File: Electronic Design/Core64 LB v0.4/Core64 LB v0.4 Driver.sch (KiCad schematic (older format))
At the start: 63 parts, among them Q4 MMBT4401LT1G

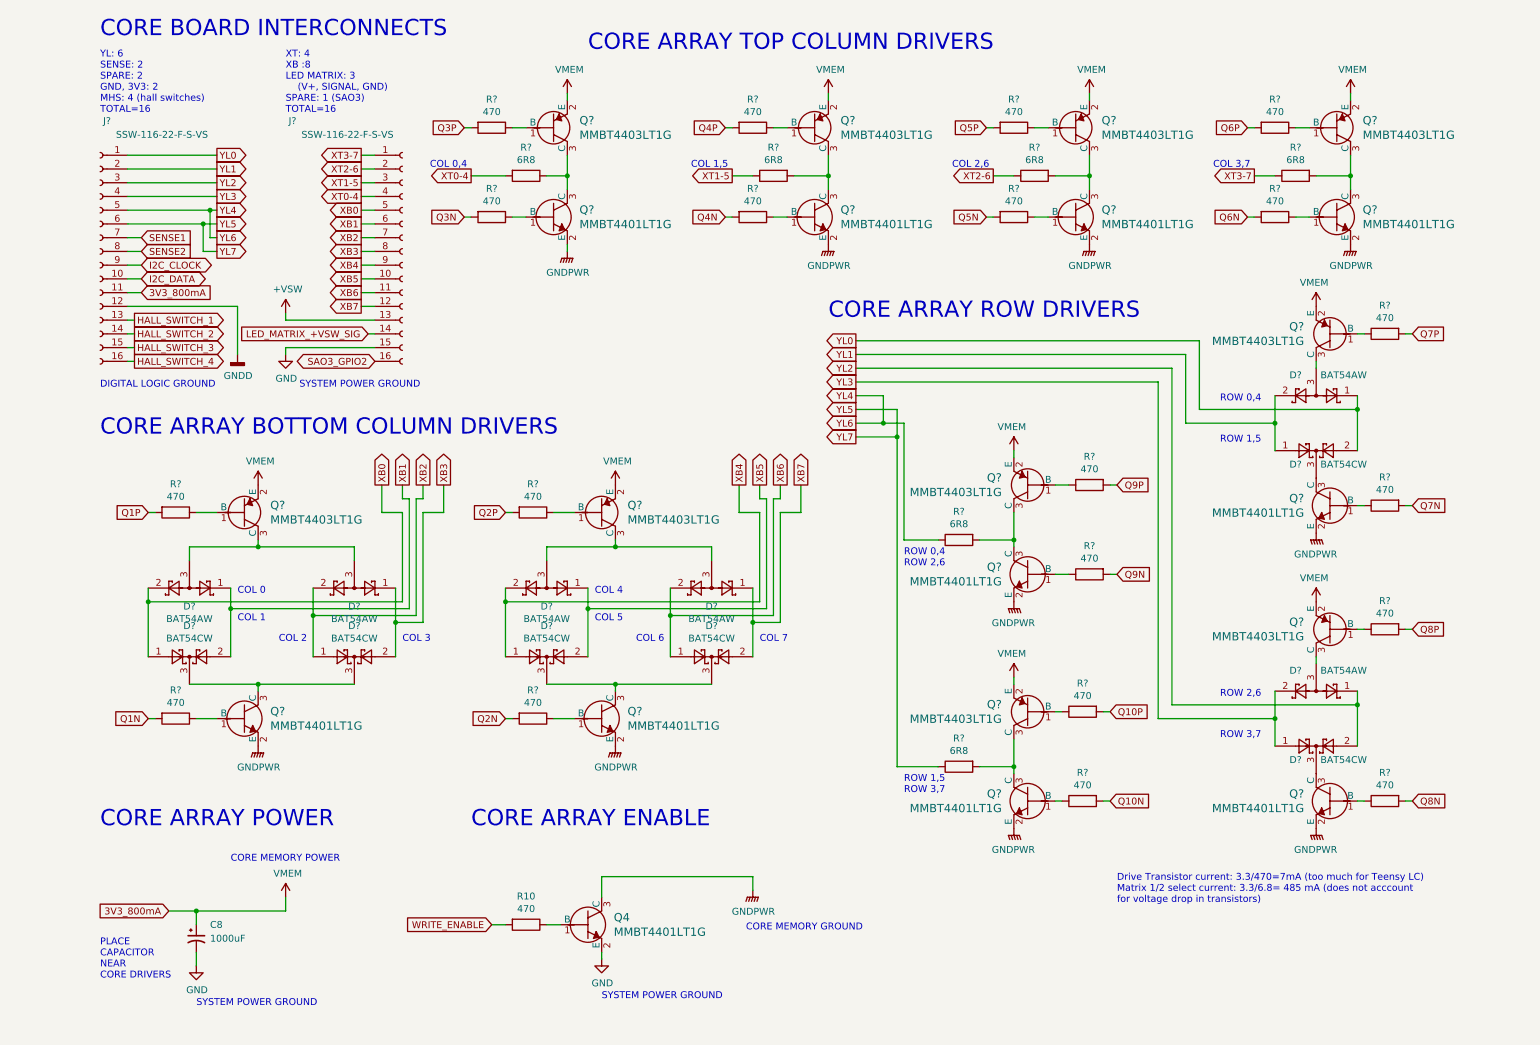
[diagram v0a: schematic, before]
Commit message: Correct Logic Board filenames to LB from CB
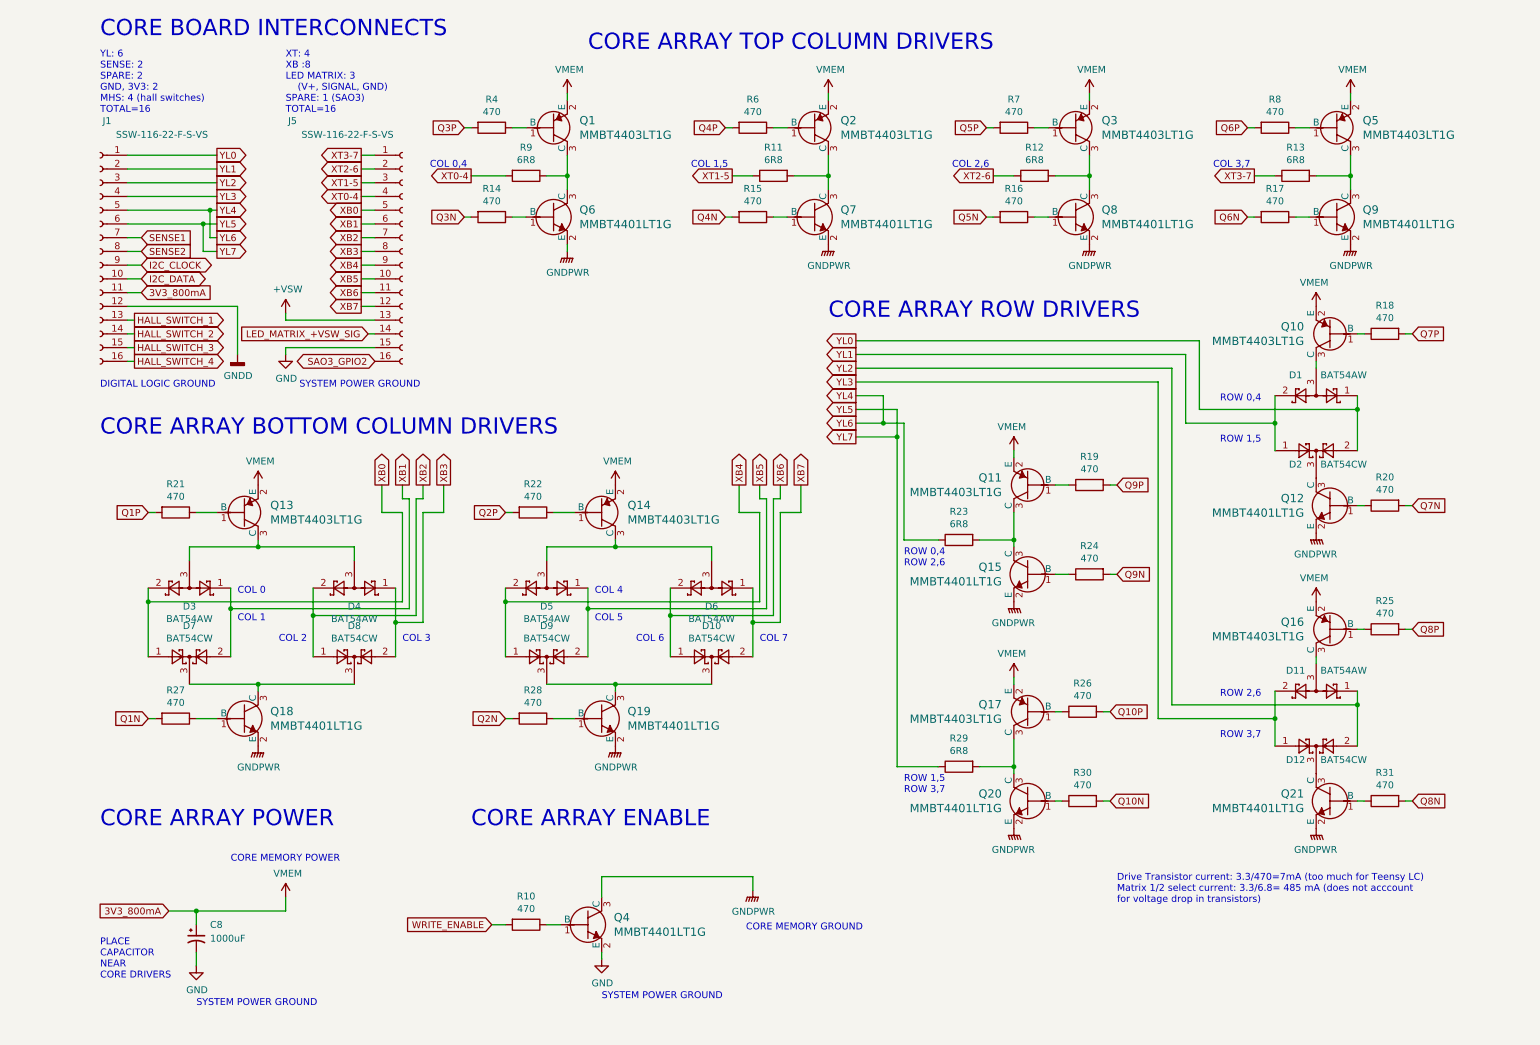
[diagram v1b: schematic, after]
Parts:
- gave numbers to parts that had none: 60

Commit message: Add regulator and battery connector data sheets, footprints, symbols
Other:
- note added: "All non-polarized capacitors are ceramic unless otherwise noted."
- note added: "TO DO: Choose BIG CAP footprint"
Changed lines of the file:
@@
 Wire Wire Line
 	3950 2250 3950 2300
+Text Notes 6300 6750 0    50   ~ 0
+All non-polarized capacitors are ceramic unless otherwise noted.
+Text Notes -100 7450 0    157  ~ 31
+TO DO: Choose BIG CAP footprint
 $EndSCHEMATC

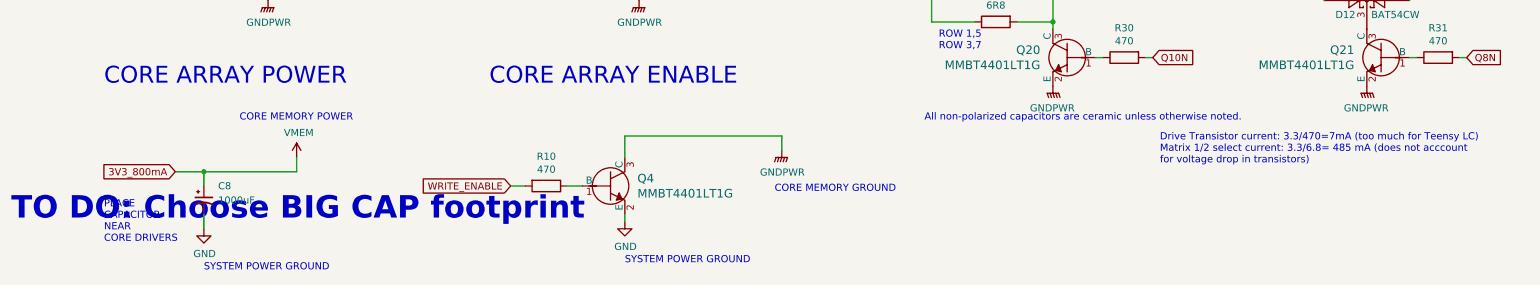
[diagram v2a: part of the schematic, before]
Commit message: Complete LB power schematic, add 3-to-8 decoder
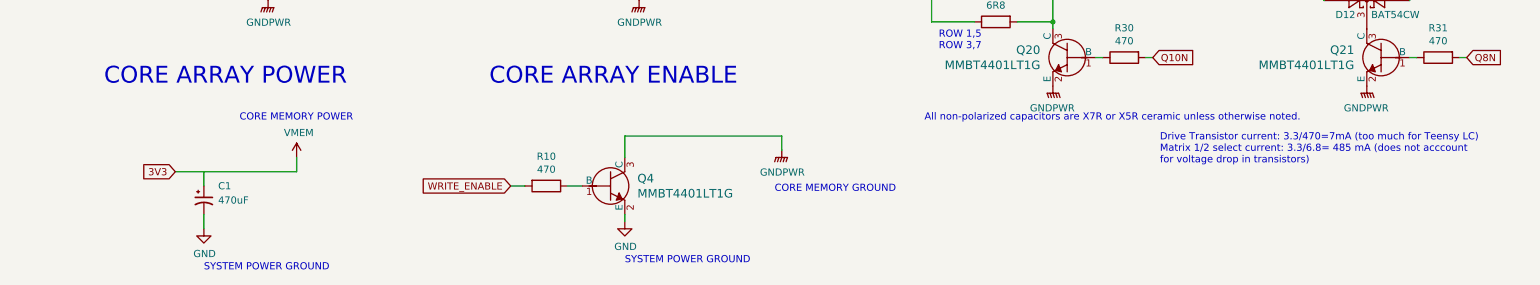
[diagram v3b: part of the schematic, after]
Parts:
- removed C8: 1000uF, Capacitor_SMD:CP_Elec_10x10, symbol Device:CP1_Small
- added C1: 470uF, Capacitor_SMD:CP_Elec_10x10, symbol Device:CP1_Small
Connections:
- net GND: now also C1.2
- net VMEM: no longer J1.11 (Pin_11)
- new net 3V3_800mA: J1.11 (Pin_11)
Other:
- note added: "All non-polarized capacitors are X7R or X5R ceramic unless otherwise noted."
- note removed: "All non-polarized capacitors are ceramic unless otherwise noted."
- note removed: "PLACE\nCAPACITOR\nNEAR\nCORE DRIVERS"
- note removed: "TO DO: Choose BIG CAP footprint"
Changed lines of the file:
@@
 CORE MEMORY POWER
 Text GLabel 1050 7100 0    50   Input ~ 0
-3V3_800mA
+3V3
 $Comp
 L power:GND #PWR?
@@
 Wire Wire Line
 	1900 2800 2550 2800
-Wire Wire Line
-	1050 7100 1250 7100
-$Comp
-L Device:CP1_Small C?
-U 1 1 5E91F406
-P 1250 7300
-AR Path="/5E755787/5E91F406" Ref="C?"  Part="1"
-AR Path="/5E755AC8/5D2551FF/5E91F406" Ref="C?"  Part="1"
-AR Path="/5E755AC8/5E91F406" Ref="C8"  Part="1"
-F 0 "C8" H 1350 7400 50  0000 L CNN
-F 1 "1000uF" H 1350 7300 50  0000 L CNN
-F 2 "Capacitor_SMD:CP_Elec_10x10" H 1250 7300 50  0001 C CNN
-F 3 "~" H 1250 7300 50  0001 C CNN
-	1    1250 7300
-	1    0    0    -1
-$EndComp
-Wire Wire Line
-	1250 7100 1250 7200
-Text Notes 550  7600 0    50   ~ 0
-PLACE\nCAPACITOR\nNEAR\nCORE DRIVERS
-Connection ~ 1250 7100
-$Comp
-L power:GND #PWR?
-U 1 1 5E94D2F4
-P 1250 7500
-AR Path="/5D254AE8/5E94D2F4" Ref="#PWR?"  Part="1"
-AR Path="/5E94D2F4" Ref="#PWR?"  Part="1"
-AR Path="/5E755AC8/5E94D2F4" Ref="#PWR0126"  Part="1"
-F 0 "#PWR0126" H 1250 7250 50  0001 C CNN
-F 1 "GND" H 1255 7325 50  0000 C CNN
-F 2 "" H 1250 7500 50  0001 C CNN
-F 3 "" H 1250 7500 50  0001 C CNN
-	1    1250 7500
-	1    0    0    -1
-$EndComp
-Text Notes 1250 7800 0    50   ~ 0
-SYSTEM POWER GROUND
-Wire Wire Line
-	1250 7400 1250 7500
 Text GLabel 850  2400 2    50   BiDi ~ 0
 I2C_CLOCK
@@
 	1900 3000 1900 3050
 Wire Wire Line
-	1250 7100 1900 7100
-Wire Wire Line
 	1700 4400 1700 4450
 Connection ~ 1700 4450
@@
 Wire Wire Line
 	3950 2250 3950 2300
+Wire Wire Line
+	1050 7100 1900 7100
+Wire Wire Line
+	1250 7100 1250 7200
+$Comp
+L power:GND #PWR?
+U 1 1 5F6C52F2
+P 1250 7500
+AR Path="/5D254AE8/5F6C52F2" Ref="#PWR?"  Part="1"
+AR Path="/5F6C52F2" Ref="#PWR?"  Part="1"
+AR Path="/5E755AC8/5F6C52F2" Ref="#PWR0118"  Part="1"
+F 0 "#PWR0118" H 1250 7250 50  0001 C CNN
+F 1 "GND" H 1255 7325 50  0000 C CNN
+F 2 "" H 1250 7500 50  0001 C CNN
+F 3 "" H 1250 7500 50  0001 C CNN
+	1    1250 7500
+	1    0    0    -1
+$EndComp
+Text Notes 1250 7800 0    50   ~ 0
+SYSTEM POWER GROUND
+Wire Wire Line
+	1250 7400 1250 7500
+$Comp
+L Device:CP1_Small C?
+U 1 1 5F6C52FB
+P 1250 7300
+AR Path="/5E755787/5F6C52FB" Ref="C?"  Part="1"
+AR Path="/5E755AC8/5D2551FF/5F6C52FB" Ref="C?"  Part="1"
+AR Path="/5E755AC8/5F6C52FB" Ref="C1"  Part="1"
+AR Path="/5E7548ED/5F6C52FB" Ref="C?"  Part="1"
+F 0 "C1" H 1350 7400 50  0000 L CNN
+F 1 "470uF" H 1350 7300 50  0000 L CNN
+F 2 "Capacitor_SMD:CP_Elec_10x10" H 1250 7300 50  0001 C CNN
+F 3 "~" H 1250 7300 50  0001 C CNN
+F 4 "565-EMHL100ARA471MHA0GCT-ND" H 1250 7300 50  0001 C CNN "Digikey"
+	1    1250 7300
+	1    0    0    -1
+$EndComp
 Text Notes 6300 6750 0    50   ~ 0
-All non-polarized capacitors are ceramic unless otherwise noted.
-Text Notes -100 7450 0    157  ~ 31
-TO DO: Choose BIG CAP footprint
+All non-polarized capacitors are X7R or X5R ceramic unless otherwise noted.
 $EndSCHEMATC

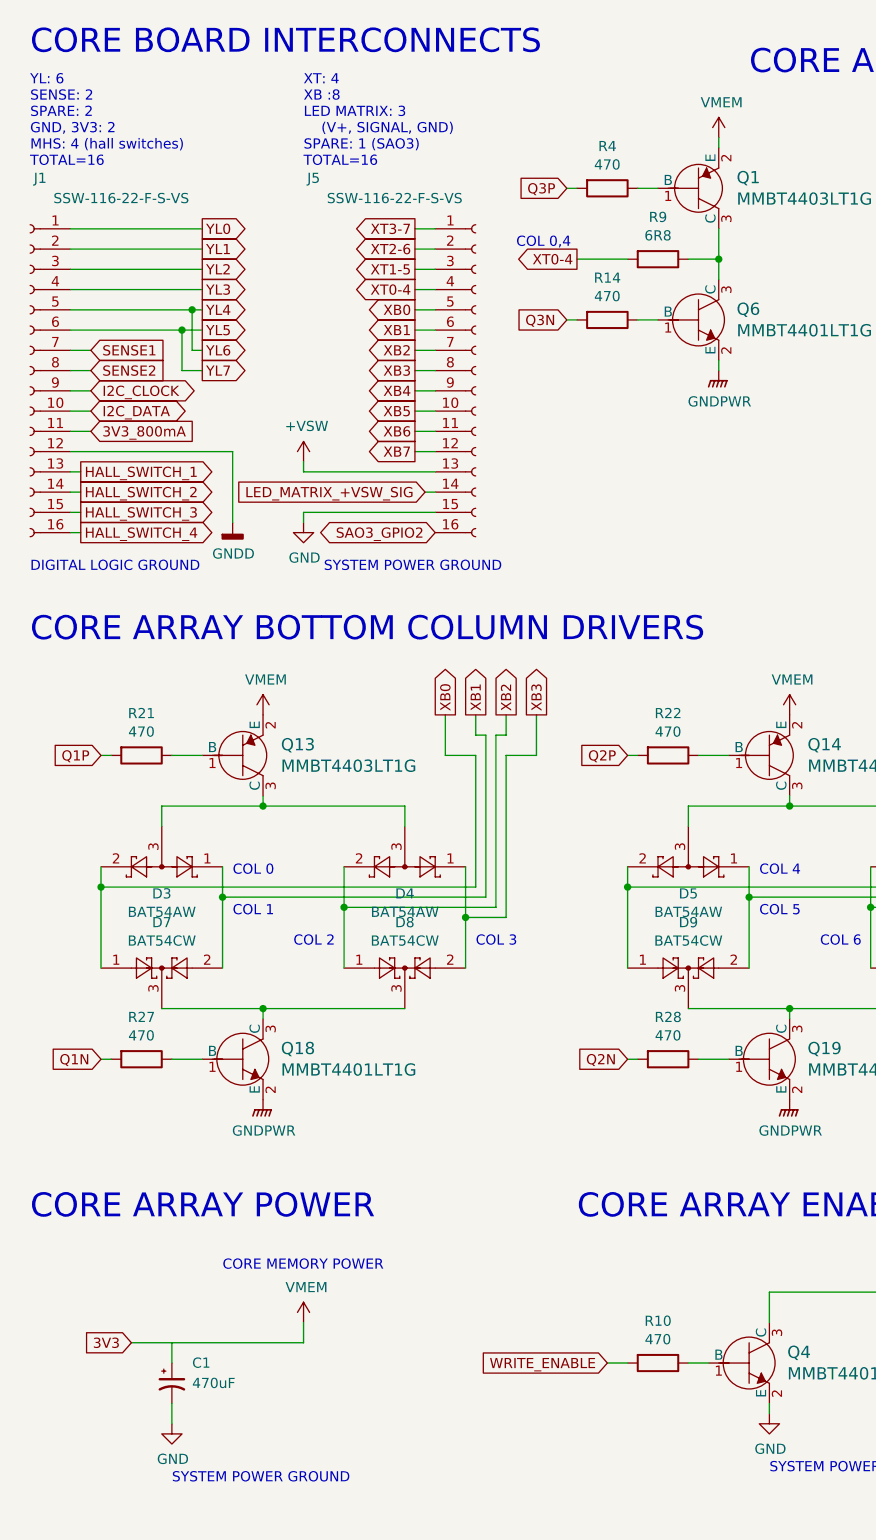
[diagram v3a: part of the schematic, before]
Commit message: Add 3-to-8 and begin other expansion on schematic
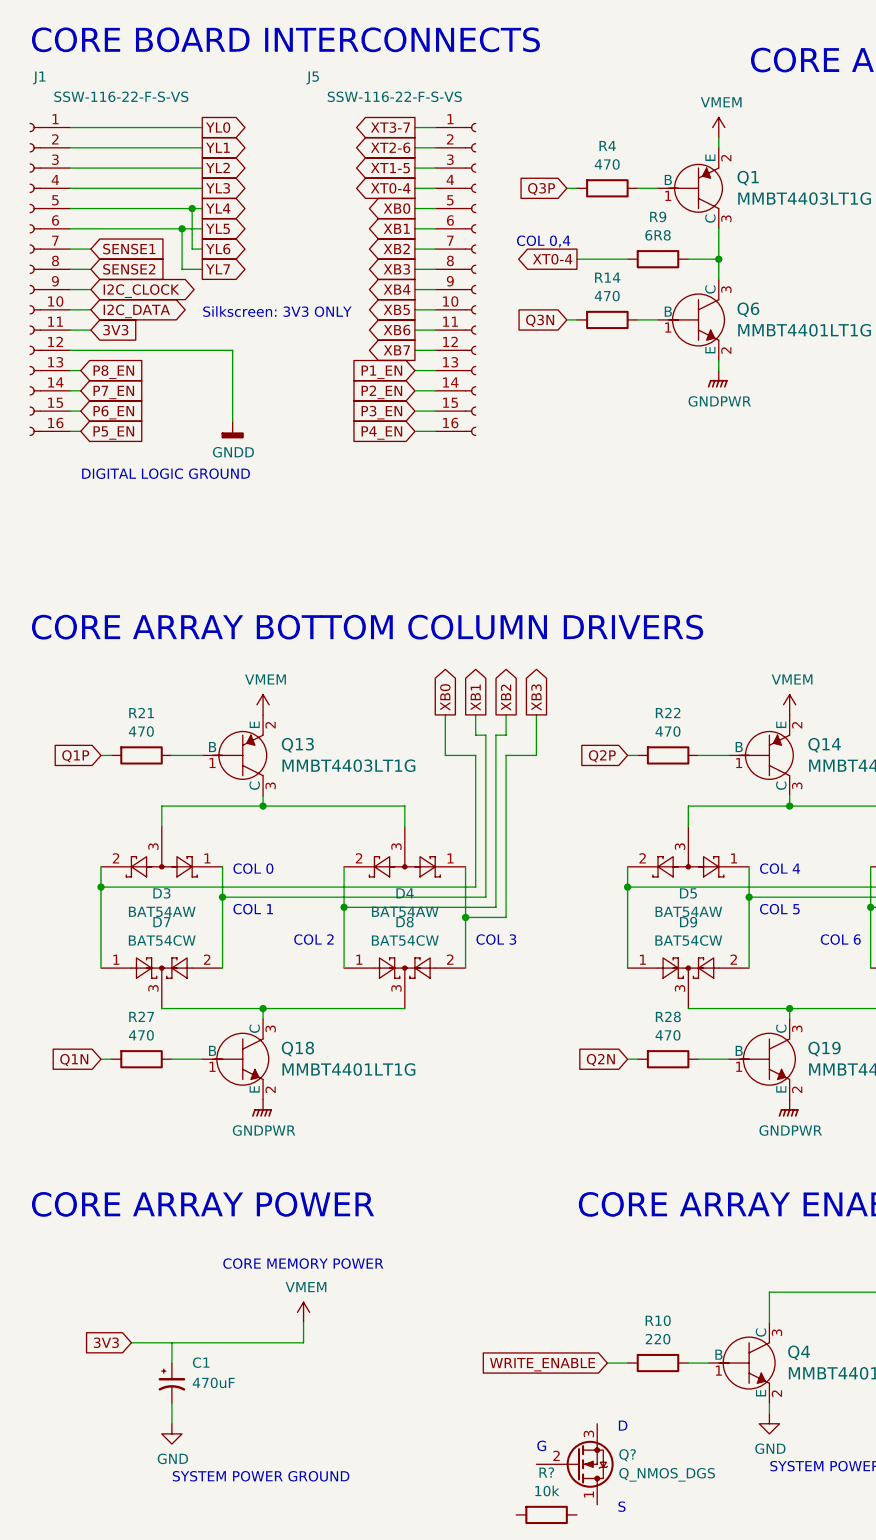
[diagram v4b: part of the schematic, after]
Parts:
- added Q?: Q_NMOS_DGS, symbol Device:Q_NMOS_DGS
- added R?: 10k, Resistor_SMD:R_0805_2012Metric, symbol Device:R
- R10: value 470 -> 220
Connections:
- net 3V3_800mA is gone; now on net VMEM: J1.11 (Pin_11)
- net GND: no longer J5.15 (Pin_15)
- net +VSW renamed P1_EN
- net HALL_SWITCH_1 renamed P8_EN
- net HALL_SWITCH_2 renamed P7_EN
- net HALL_SWITCH_3 renamed P6_EN
- net HALL_SWITCH_4 renamed P5_EN
- net LED_MATRIX_+VSW_SIG renamed P2_EN
- net SAO3_GPIO2 renamed P4_EN
- new net P3_EN: J5.15 (Pin_15)
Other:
- note added: "D"
- note added: "G"
- note added: "S"
- note added: "Silkscreen: 3V3 ONLY"
- note removed: "XT: 4\nXB :8\nLED MATRIX: 3\n (V+, SIGNAL, GND)\nSPARE: 1 (SAO3)\nTOTAL=16"
- note removed: "YL: 6\nSENSE: 2\nSPARE: 2\nGND, 3V3: 2\nMHS: 4 (hall switches)\nTOTAL=16"
- moved on the sheet: J1, J5
